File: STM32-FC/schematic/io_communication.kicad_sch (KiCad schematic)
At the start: 40 parts, among them J10 SM06B-GHS-TBT, J11 SM06B-GHS-TBT, J12 PWM_Conn_3x14, J13 SM04B-GHS-TBT, J14 ZH 1.5mm 4P, J15 SM06B-GHS-TBT, J5 SM06B-GHS-TBT, J6 SM06B-GHS-TBT, J7 SM04B-GHS-TBT, J8 SM04B-GHS-TBT, J9 SM04B-GHS-TBT, Q1 PMDPB30XN, U11 ATA6561-GBQW, U12 ATA6561-GBQW, U13 TMUX1104

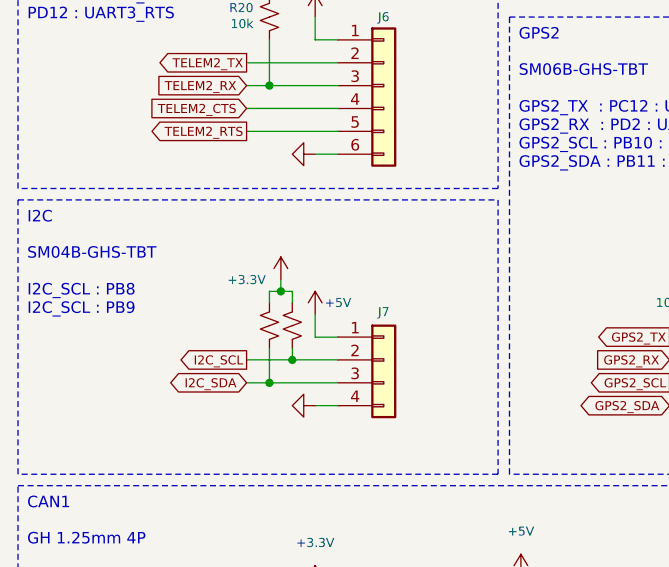
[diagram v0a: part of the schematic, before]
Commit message: fix : BMM350 power 1.8V and add dc2dc converter for 1.8V
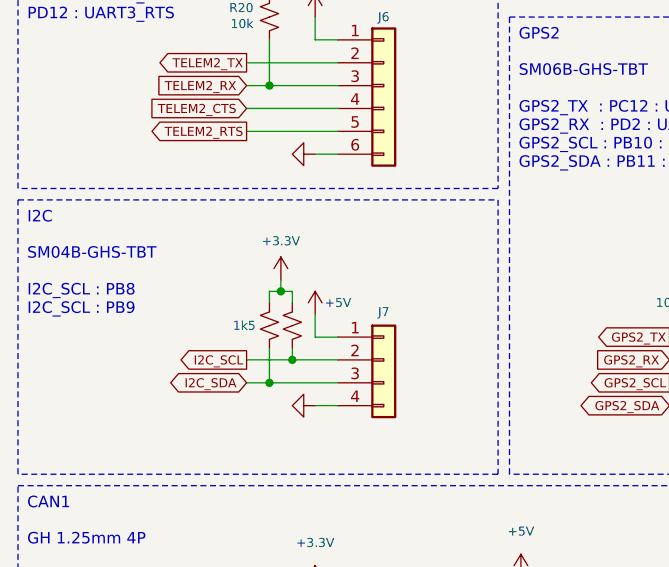
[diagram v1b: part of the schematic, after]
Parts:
- R21, R22: value 10k -> 1k5; LCSC C25531 -> C25867
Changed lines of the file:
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@@
 			)
 		)
-		(property "Value" "10k"
-			(at 43.688 101.6 0)
+		(property "Value" "1k5"
+			(at 49.276 100.33 0)
 			(effects
 				(font
@@
 				)
 				(justify left)
-				(hide yes)
 			)
 		)
@@
 			)
 		)
-		(property "LCSC" "C25531"
+		(property "LCSC" "C25867"
 			(at 50.8 100.33 0)
 			(effects
@@
 		)
 		(property "Value" "+3.3V"
-			(at 48.26 95.25 0)
+			(at 52.07 90.932 0)
 			(effects
 				(font
@@
 			)
 		)
-		(property "Value" "10k"
-			(at 46.228 101.6 0)
+		(property "Value" "1k5"
+			(at 49.022 99.568 0)
 			(effects
 				(font
@@
 			)
 		)
-		(property "LCSC" "C25531"
+		(property "LCSC" "C25867"
 			(at 53.34 100.33 0)
 			(effects

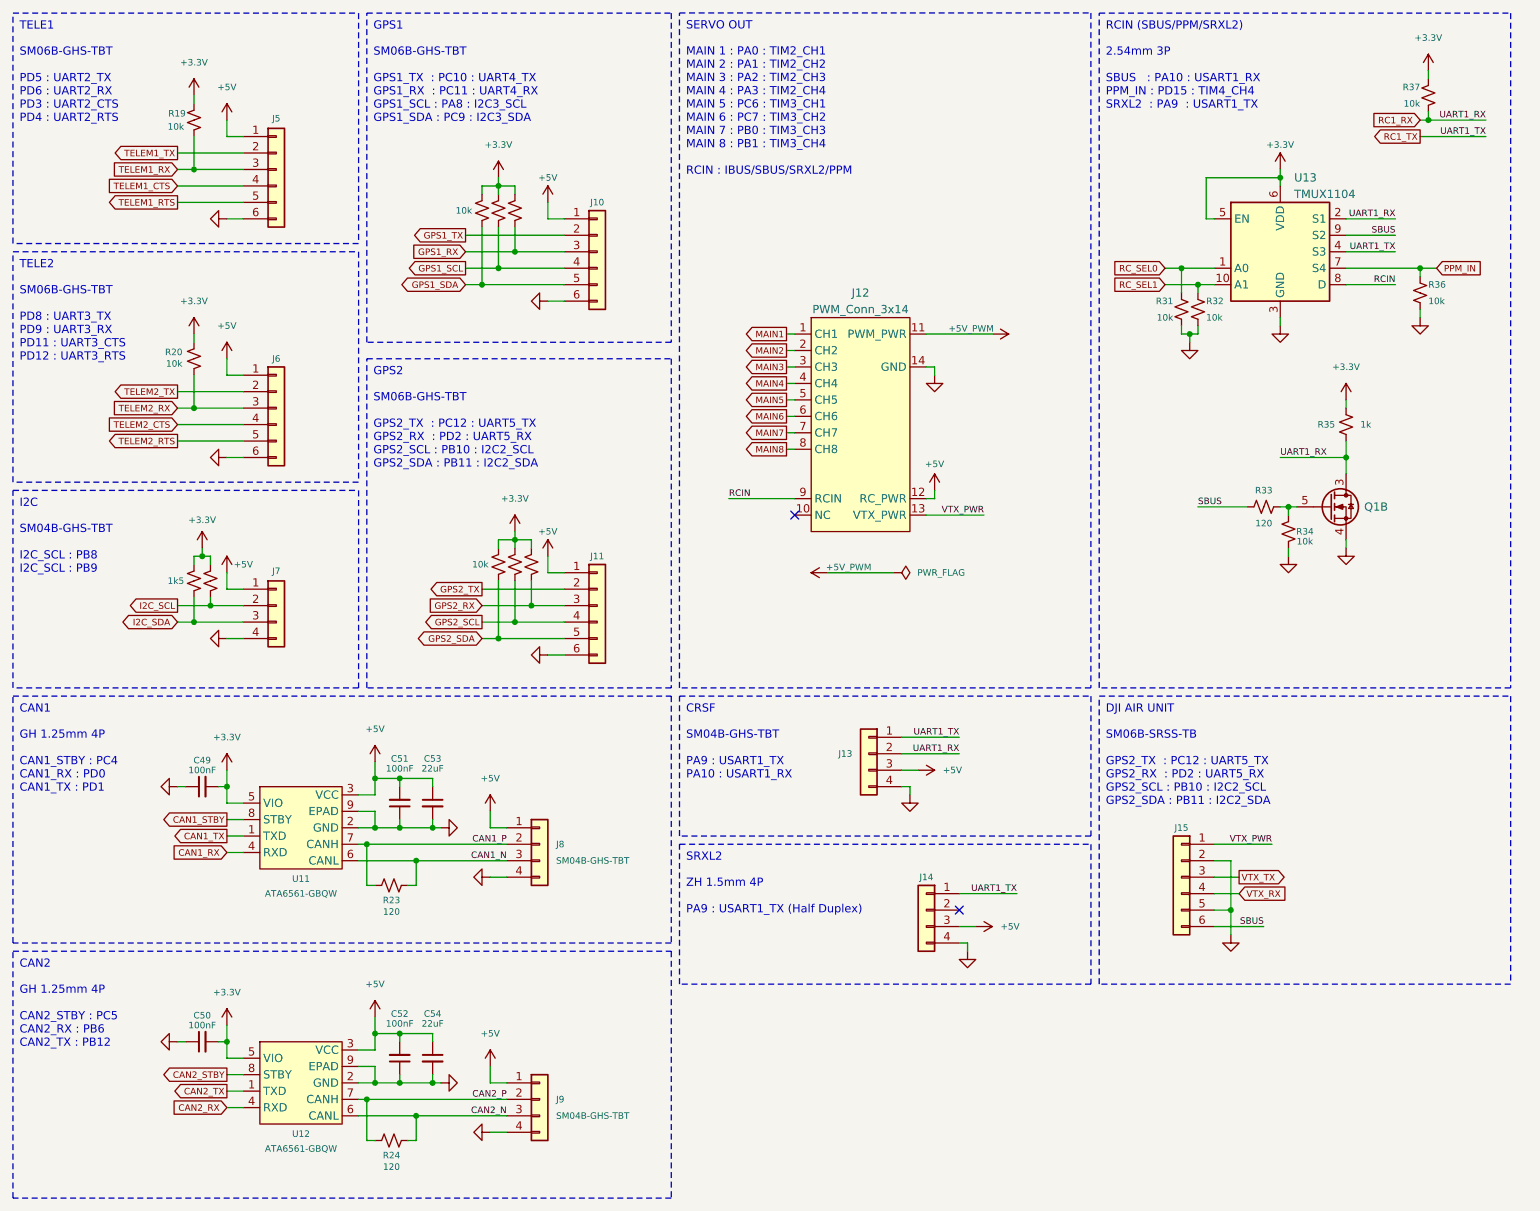
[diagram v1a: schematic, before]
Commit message: update : BOM and minor fix
- remove : DC2DC for analog
- change : JST SM conn. to BM
- change : ELRS conn. to JST XH (instead of JST SM)
- update : BOM List
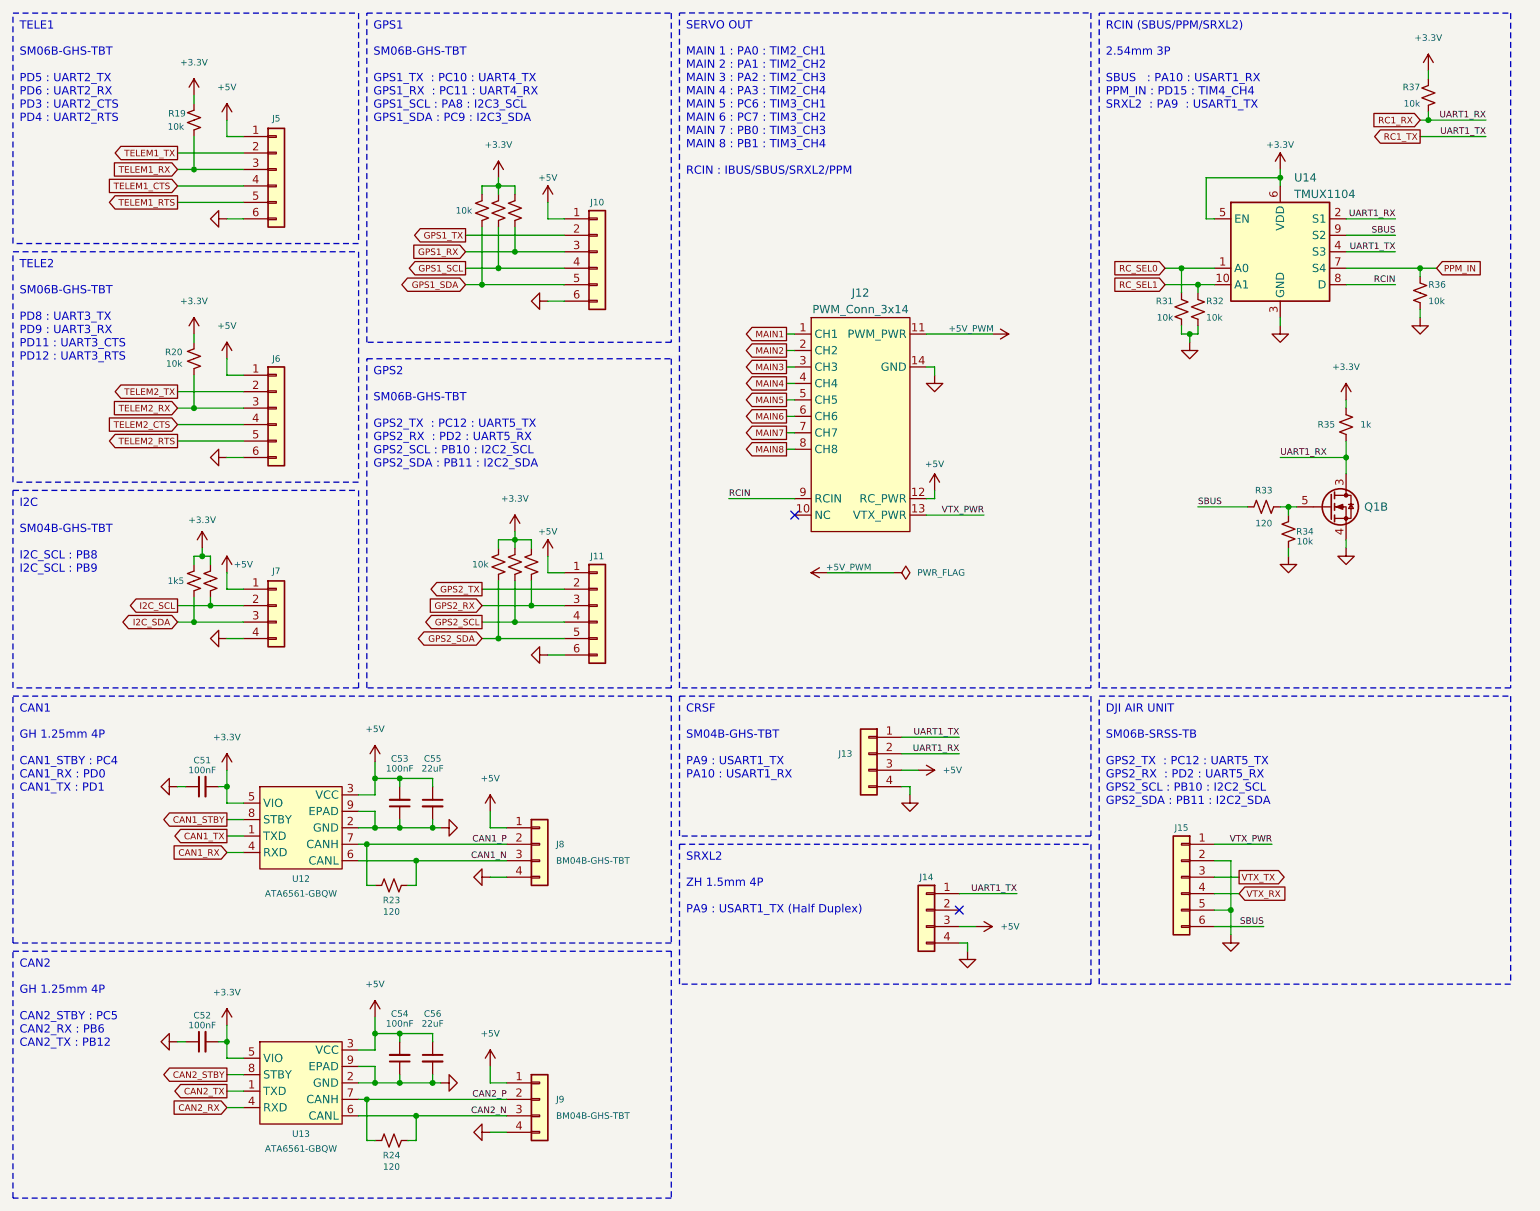
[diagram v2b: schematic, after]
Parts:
- J10, J11, J5, J6: value SM06B-GHS-TBT -> BM06B-GHS-TBT; footprint Connector_JST:JST_GH_SM06B-GHS-TB_1x06-1MP_P1.25mm_Horizontal -> Connector_JST:JST_GH_BM06B-GHS-TBT_1x06-1MP_P1.25mm_Vertical; LCSC C133065 -> C189892
- J13, J7, J8, J9: value SM04B-GHS-TBT -> BM04B-GHS-TBT; footprint Connector_JST:JST_GH_SM04B-GHS-TB_1x04-1MP_P1.25mm_Horizontal -> Connector_JST:JST_GH_BM04B-GHS-TBT_1x04-1MP_P1.25mm_Vertical; LCSC C189895 -> C161692
- J15: value SM06B-GHS-TBT -> BM06B-GHS-TBT; footprint Connector_JST:JST_GH_SM06B-GHS-TB_1x06-1MP_P1.25mm_Horizontal -> Connector_JST:JST_GH_BM06B-GHS-TBT_1x06-1MP_P1.25mm_Vertical; LCSC C160405 -> C189892
- renumbered C49 to C51, C50 to C52, C51 to C53, C52 to C54, C53 to C55, C54 to C56, U11 to U12, U12 to U13, U13 to U14

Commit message: change : RC size 0402 to 0201
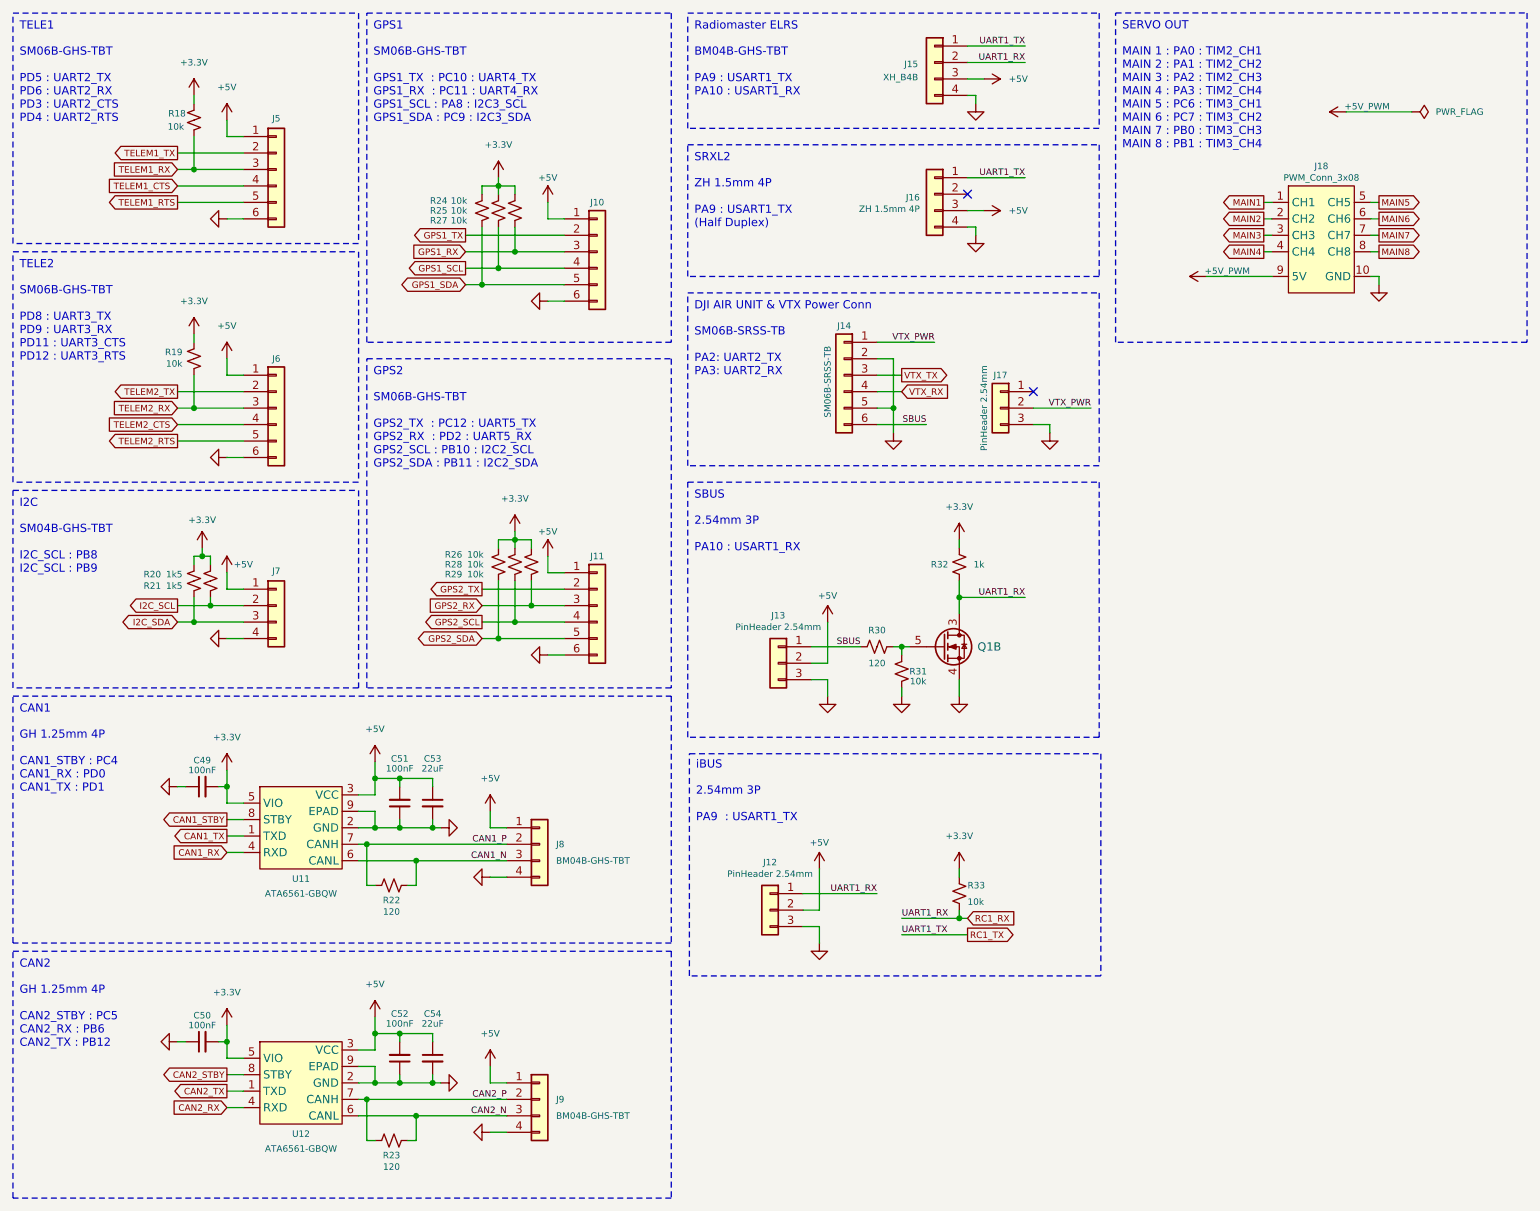
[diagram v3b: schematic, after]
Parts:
- removed J12: PWM_Conn_3x14, PWM_Connector:PWM_Conn_3x14, symbol PWM_Connector:PWM_Conn_3x10
- removed R31, R32, R36: 10k, Resistor_SMD:R_0402_1005Metric, symbol Device:R_Small_US
- removed U14: TMUX1104, Package_SON:USON-10_2.5x1.0mm_P0.5mm, symbol TMUX1104:TMUX1104
- added J12, J13, J17: PinHeader 2.54mm, Connector_PinHeader_2.54mm:PinHeader_1x03_P2.54mm_Vertical, symbol Connector_Generic:Conn_01x03
- added J18: PWM_Conn_3x08, PWM_Connector:PWM_Conn_3x08, symbol PWM_Connector:PWM_Conn_3x08
- C49: renamed from C51; footprint Capacitor_SMD:C_0402_1005Metric -> Capacitor_SMD:C_0201_0603Metric; LCSC C1525 -> C49062
- C50: renamed from C52; footprint Capacitor_SMD:C_0402_1005Metric -> Capacitor_SMD:C_0201_0603Metric; LCSC C1525 -> C49062
- C51: renamed from C53; footprint Capacitor_SMD:C_0402_1005Metric -> Capacitor_SMD:C_0201_0603Metric; LCSC C1525 -> C49062
- C52: renamed from C54; footprint Capacitor_SMD:C_0402_1005Metric -> Capacitor_SMD:C_0201_0603Metric; LCSC C1525 -> C49062
- J14: renamed from J15; value BM06B-GHS-TBT -> SM06B-SRSS-TB; footprint Connector_JST:JST_GH_BM06B-GHS-TBT_1x06-1MP_P1.25mm_Vertical -> Connector_JST:JST_SH_SM06B-SRSS-TB_1x06-1MP_P1.00mm_Horizontal; LCSC C189892 -> C160405
- J15: renamed from J13; value BM04B-GHS-TBT -> XH_B4B; footprint Connector_JST:JST_GH_BM04B-GHS-TBT_1x04-1MP_P1.25mm_Vertical -> Connector_JST:JST_XH_B4B-XH-AM_1x04_P2.50mm_Vertical; LCSC C161692 -> C37815
- R18: renamed from R19; footprint Resistor_SMD:R_0402_1005Metric -> Resistor_SMD:R_0201_0603Metric; LCSC C25531 -> C106225
- R19: renamed from R20; footprint Resistor_SMD:R_0402_1005Metric -> Resistor_SMD:R_0201_0603Metric; LCSC C25531 -> C106225
- R22: renamed from R23; footprint Resistor_SMD:R_0402_1005Metric -> Resistor_SMD:R_0201_0603Metric; LCSC C25079 -> C295718
- R23: renamed from R24; footprint Resistor_SMD:R_0402_1005Metric -> Resistor_SMD:R_0201_0603Metric; LCSC C25079 -> C295718
- R24: renamed from R25; footprint Resistor_SMD:R_0402_1005Metric -> Resistor_SMD:R_0201_0603Metric; LCSC C25531 -> C106225
- R25: renamed from R26; footprint Resistor_SMD:R_0402_1005Metric -> Resistor_SMD:R_0201_0603Metric; LCSC C25531 -> C106225
- R26: renamed from R27; footprint Resistor_SMD:R_0402_1005Metric -> Resistor_SMD:R_0201_0603Metric; LCSC C25531 -> C106225
- R27: renamed from R28; footprint Resistor_SMD:R_0402_1005Metric -> Resistor_SMD:R_0201_0603Metric; LCSC C25531 -> C106225
- R28: renamed from R29; footprint Resistor_SMD:R_0402_1005Metric -> Resistor_SMD:R_0201_0603Metric; LCSC C25531 -> C106225
- R29: renamed from R30; footprint Resistor_SMD:R_0402_1005Metric -> Resistor_SMD:R_0201_0603Metric; LCSC C25531 -> C106225
- R30: renamed from R33; footprint Resistor_SMD:R_0402_1005Metric -> Resistor_SMD:R_0201_0603Metric; LCSC C25079 -> C295718
- R31: renamed from R34; footprint Resistor_SMD:R_0402_1005Metric -> Resistor_SMD:R_0201_0603Metric; LCSC C25531 -> C106225
- R33: renamed from R37; footprint Resistor_SMD:R_0402_1005Metric -> Resistor_SMD:R_0201_0603Metric; LCSC C25531 -> C106225
- renumbered C55 to C53, C56 to C54, J14 to J16, R21 to R20, R22 to R21, R35 to R32, U12 to U11, U13 to U12
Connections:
- net +5V: now also J12.2 (Pin_2), J13.2 (Pin_2)
- net +5V_PWM: now also J18.9 (5V)
- net GND: now also J12.3 (Pin_3), J13.3 (Pin_3), J17.3 (Pin_3), J18.10 (GND)
- net MAIN1: now also J18.1 (CH1)
- net MAIN2: now also J18.2 (CH2)
- net MAIN3: now also J18.3 (CH3)
- net MAIN4: now also J18.4 (CH4)
- net MAIN5: now also J18.5 (CH5)
- net MAIN6: now also J18.6 (CH6)
- net MAIN7: now also J18.7 (CH7)
- net MAIN8: now also J18.8 (CH8)
- net RC1_RX: now also J12.1 (Pin_1)
- net SBUS: now also J13.1 (Pin_1)
- net VTX_PWR: now also J17.2 (Pin_2)
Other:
- note added: "2.54mm 3P PA10 : USART1_RX"
- note added: "2.54mm 3P PA9 : USART1_TX"
- note added: "BM04B-GHS-TBT PA9 : USART1_TX PA10 : USART1_RX"
- note added: "DJI AIR UNIT & VTX Power Conn"
- note added: "MAIN 1 : PA0 : TIM2_CH1 MAIN 2 : PA1 : TIM2_CH2 MAIN 3 : PA2 : TIM2_CH3 MAIN 4 : PA3 : TIM2_CH4 MAIN 5 : PC6 : TIM3_CH1 MAIN 6 : PC7 : TIM3_CH2 MAIN 7 : PB0 : TIM3_CH3 MAIN 8 : PB1 : TIM3_CH4"
- note added: "Radiomaster ELRS"
- note added: "SBUS"
- note added: "SM06B-SRSS-TB PA2: UART2_TX PA3: UART2_RX"
- note added: "iBUS"
- note removed: "2.54mm 3P SBUS : PA10 : USART1_RX PPM_IN : PD15 : TIM4_CH4 SRXL2 : PA9 : USART1_TX"
- note removed: "CRSF"
- note removed: "DJI AIR UNIT"
- note removed: "MAIN 1 : PA0 : TIM2_CH1 MAIN 2 : PA1 : TIM2_CH2 MAIN 3 : PA2 : TIM2_CH3 MAIN 4 : PA3 : TIM2_CH4 MAIN 5 : PC6 : TIM3_CH1 MAIN 6 : PC7 : TIM3_CH2 MAIN 7 : PB0 : TIM3_CH3 MAIN 8 : PB1 : TIM3_CH4 RCIN : IBUS/SBUS/SRXL2/PPM"
- note removed: "RCIN (SBUS/PPM/SRXL2)"
- note removed: "SM04B-GHS-TBT PA9 : USART1_TX PA10 : USART1_RX"
- note removed: "SM06B-SRSS-TB GPS2_TX : PC12 : UART5_TX GPS2_RX : PD2 : UART5_RX GPS2_SCL : PB10 : I2C2_SCL GPS2_SDA : PB11 : I2C2_SDA"
- moved on the sheet: J14, J15, J16, Q1B, R30, R31, R32, R33
